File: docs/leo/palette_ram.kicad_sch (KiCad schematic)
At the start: 15 parts, among them IC10 74LS273, IC15 MB81C78A, IC16 MB81C78A, IC17 74153, IC18 74153, IC19 74153, IC22 74LS245, IC23 74LS245, IC25 74153, IC26 74153, IC27 74153, IC28 74153, IC30 74LS374, IC31 74LS374, IC9 74LS273

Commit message: Renamed shared ram
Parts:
- IC10, IC9: value 74LS273 -> (none)
- IC15, IC16: value MB81C78A -> (none); footprint Package_DIP:DIP-28_W15.24mm -> (none)
- IC17, IC18, IC19, IC25, IC26, IC27, IC28: value 74153 -> (none)
- IC22, IC23: value 74LS245 -> (none)
- IC30, IC31: value 74LS374 -> (none)
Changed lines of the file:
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@@
     (in_bom yes) (on_board yes) (fields_autoplaced)
     (property "Reference" "IC17" (id 0) (at 58.42 22.86 0))
-    (property "Value" "74153" (id 1) (at 58.42 25.4 0))
+    (property "Value" "" (id 1) (at 58.42 25.4 0))
     (property "Footprint" "" (id 2) (at 58.42 46.99 0)
       (effects (font (size 1.27 1.27)) hide)
@@
     (in_bom yes) (on_board yes) (fields_autoplaced)
     (property "Reference" "IC19" (id 0) (at 58.42 109.22 0))
-    (property "Value" "74153" (id 1) (at 58.42 111.76 0))
+    (property "Value" "" (id 1) (at 58.42 111.76 0))
     (property "Footprint" "" (id 2) (at 58.42 133.35 0)
       (effects (font (size 1.27 1.27)) hide)
@@
       (effects (font (size 1.27 1.27)) (justify right))
     )
-    (property "Value" "74LS273" (id 1) (at 258.3306 193.04 0)
+    (property "Value" "" (id 1) (at 258.3306 193.04 0)
       (effects (font (size 1.27 1.27)) (justify right))
     )
@@
       (effects (font (size 1.27 1.27)) (justify left))
     )
-    (property "Value" "74LS245" (id 1) (at 391.9094 48.26 0)
+    (property "Value" "" (id 1) (at 391.9094 48.26 0)
       (effects (font (size 1.27 1.27)) (justify left))
     )
@@
       (effects (font (size 1.27 1.27)) (justify right))
     )
-    (property "Value" "74LS374" (id 1) (at 390.4106 193.04 0)
+    (property "Value" "" (id 1) (at 390.4106 193.04 0)
       (effects (font (size 1.27 1.27)) (justify right))
     )
@@
       (effects (font (size 1.27 1.27)) (justify left))
     )
-    (property "Value" "MB81C78A" (id 1) (at 259.8294 48.26 0)
-      (effects (font (size 1.27 1.27)) (justify left))
-    )
-    (property "Footprint" "Package_DIP:DIP-28_W15.24mm" (id 2) (at 278.13 95.25 0)
+    (property "Value" "" (id 1) (at 259.8294 48.26 0)
+      (effects (font (size 1.27 1.27)) (justify left))
+    )
+    (property "Footprint" "" (id 2) (at 278.13 95.25 0)
       (effects (font (size 1.27 1.27)) hide)
     )
@@
       (effects (font (size 1.27 1.27)) (justify right))
     )
-    (property "Value" "74LS273" (id 1) (at 258.3306 246.38 0)
+    (property "Value" "" (id 1) (at 258.3306 246.38 0)
       (effects (font (size 1.27 1.27)) (justify right))
     )
@@
       (effects (font (size 1.27 1.27)) (justify left))
     )
-    (property "Value" "74LS245" (id 1) (at 391.9094 93.98 0)
+    (property "Value" "" (id 1) (at 391.9094 93.98 0)
       (effects (font (size 1.27 1.27)) (justify left))
     )
@@
     (in_bom yes) (on_board yes) (fields_autoplaced)
     (property "Reference" "IC28" (id 0) (at 133.35 152.4 0))
-    (property "Value" "74153" (id 1) (at 133.35 154.94 0))
+    (property "Value" "" (id 1) (at 133.35 154.94 0))
     (property "Footprint" "" (id 2) (at 133.35 176.53 0)
       (effects (font (size 1.27 1.27)) hide)
@@
     (in_bom yes) (on_board yes) (fields_autoplaced)
     (property "Reference" "IC18" (id 0) (at 58.42 66.04 0))
-    (property "Value" "74153" (id 1) (at 58.42 68.58 0))
+    (property "Value" "" (id 1) (at 58.42 68.58 0))
     (property "Footprint" "" (id 2) (at 58.42 90.17 0)
       (effects (font (size 1.27 1.27)) hide)
@@
       (effects (font (size 1.27 1.27)) hide)
     )
-    (property "Value" "GND" (id 1) (at 313.69 180.34 0))
+    (property "Value" "" (id 1) (at 313.69 180.34 0))
     (property "Footprint" "" (id 2) (at 313.69 175.26 0)
       (effects (font (size 1.27 1.27)) hide)
@@
     (in_bom yes) (on_board yes) (fields_autoplaced)
     (property "Reference" "IC27" (id 0) (at 133.35 109.22 0))
-    (property "Value" "74153" (id 1) (at 133.35 111.76 0))
+    (property "Value" "" (id 1) (at 133.35 111.76 0))
     (property "Footprint" "" (id 2) (at 133.35 133.35 0)
       (effects (font (size 1.27 1.27)) hide)
@@
       (effects (font (size 1.27 1.27)) (justify left))
     )
-    (property "Value" "MB81C78A" (id 1) (at 259.8294 116.84 0)
-      (effects (font (size 1.27 1.27)) (justify left))
-    )
-    (property "Footprint" "Package_DIP:DIP-28_W15.24mm" (id 2) (at 278.13 163.83 0)
+    (property "Value" "" (id 1) (at 259.8294 116.84 0)
+      (effects (font (size 1.27 1.27)) (justify left))
+    )
+    (property "Footprint" "" (id 2) (at 278.13 163.83 0)
       (effects (font (size 1.27 1.27)) hide)
     )
@@
       (effects (font (size 1.27 1.27)) hide)
     )
-    (property "Value" "GND" (id 1) (at 95.25 213.36 0))
+    (property "Value" "" (id 1) (at 95.25 213.36 0))
     (property "Footprint" "" (id 2) (at 95.25 208.28 0)
       (effects (font (size 1.27 1.27)) hide)
@@
     (in_bom yes) (on_board yes) (fields_autoplaced)
     (property "Reference" "IC26" (id 0) (at 133.35 66.04 0))
-    (property "Value" "74153" (id 1) (at 133.35 68.58 0))
+    (property "Value" "" (id 1) (at 133.35 68.58 0))
     (property "Footprint" "" (id 2) (at 133.35 90.17 0)
       (effects (font (size 1.27 1.27)) hide)
@@
       (effects (font (size 1.27 1.27)) hide)
     )
-    (property "Value" "VCC" (id 1) (at 223.52 33.02 0))
+    (property "Value" "" (id 1) (at 223.52 33.02 0))
     (property "Footprint" "" (id 2) (at 223.52 38.1 0)
       (effects (font (size 1.27 1.27)) hide)
@@
       (effects (font (size 1.27 1.27)) hide)
     )
-    (property "Value" "VCC" (id 1) (at 100.33 170.18 0))
+    (property "Value" "" (id 1) (at 100.33 170.18 0))
     (property "Footprint" "" (id 2) (at 100.33 175.26 0)
       (effects (font (size 1.27 1.27)) hide)
@@
       (effects (font (size 1.27 1.27)) (justify right))
     )
-    (property "Value" "74LS374" (id 1) (at 390.4106 147.32 0)
+    (property "Value" "" (id 1) (at 390.4106 147.32 0)
       (effects (font (size 1.27 1.27)) (justify right))
     )
@@
       (effects (font (size 1.27 1.27)) hide)
     )
-    (property "Value" "GND" (id 1) (at 22.86 213.36 0))
+    (property "Value" "" (id 1) (at 22.86 213.36 0))
     (property "Footprint" "" (id 2) (at 22.86 208.28 0)
       (effects (font (size 1.27 1.27)) hide)
@@
     (in_bom yes) (on_board yes) (fields_autoplaced)
     (property "Reference" "IC25" (id 0) (at 133.35 22.86 0))
-    (property "Value" "74153" (id 1) (at 133.35 25.4 0))
+    (property "Value" "" (id 1) (at 133.35 25.4 0))
     (property "Footprint" "" (id 2) (at 133.35 46.99 0)
       (effects (font (size 1.27 1.27)) hide)

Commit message: schematic updates
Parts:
- IC10, IC9: value (none) -> 74LS273
- IC15, IC16: value (none) -> MB81C78A; footprint (none) -> Package_DIP:DIP-28_W15.24mm
- IC17, IC18, IC19, IC25, IC26, IC27, IC28: value (none) -> 74153
- IC22, IC23: value (none) -> 74LS245
- IC30, IC31: value (none) -> 74LS374
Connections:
- net D0: now also IC30.19 (O7); no longer IC30.2 (O0)
- net D1: now also IC30.16 (O6); no longer IC30.5 (O1)
- net D10: now also IC31.15 (O5); no longer IC31.6 (O2)
- net D11: now also IC31.12 (O4); no longer IC31.9 (O3)
- net D12: now also IC31.9 (O3); no longer IC31.12 (O4)
- net D13: now also IC31.6 (O2); no longer IC31.15 (O5)
- net D14: now also IC31.5 (O1); no longer IC31.16 (O6)
- net D15: now also IC31.2 (O0); no longer IC31.19 (O7)
- net D2: now also IC30.15 (O5); no longer IC30.6 (O2)
- net D3: now also IC30.12 (O4); no longer IC30.9 (O3)
- net D4: now also IC30.9 (O3); no longer IC30.12 (O4)
- net D5: now also IC30.6 (O2); no longer IC30.15 (O5)
- net D6: now also IC30.5 (O1); no longer IC30.16 (O6)
- net D7: now also IC30.2 (O0); no longer IC30.19 (O7)
- net D8: now also IC31.19 (O7); no longer IC31.2 (O0)
- net D9: now also IC31.16 (O6); no longer IC31.5 (O1)
- net BUFFER_D11: now reaches IC31.13 (D4)
- net BUFFER_D10: now reaches IC31.14 (D5)
- net BUFFER_D9: now reaches IC31.17 (D6)
- net BUFFER_D8: now reaches IC31.18 (D7)
- net BUFFER_D15: now reaches IC31.3 (D0)
- net BUFFER_D14: now reaches IC31.4 (D1)
- net BUFFER_D13: now reaches IC31.7 (D2)
- net BUFFER_D12: now reaches IC31.8 (D3)
- net BUFFER_D3: now reaches IC30.13 (D4)
- net BUFFER_D2: now reaches IC30.14 (D5)
- net BUFFER_D1: now reaches IC30.17 (D6)
- net BUFFER_D0: now reaches IC30.18 (D7)
- net BUFFER_D7: now reaches IC30.3 (D0)
- net BUFFER_D6: now reaches IC30.4 (D1)
- net BUFFER_D5: now reaches IC30.7 (D2)
- net BUFFER_D4: now reaches IC30.8 (D3)
- net BUF_D0 renamed CPU_D0
- net BUF_D1 renamed CPU_D1
- net BUF_D10 renamed CPU_D10
- net BUF_D11 renamed CPU_D11
- net BUF_D12 renamed CPU_D12
- net BUF_D13 renamed CPU_D13
- net BUF_D14 renamed CPU_D14
- net BUF_D15 renamed CPU_D15
- net BUF_D2 renamed CPU_D2
- net BUF_D3 renamed CPU_D3
- net BUF_D4 renamed CPU_D4
- net BUF_D5 renamed CPU_D5
- net BUF_D6 renamed CPU_D6
- net BUF_D7 renamed CPU_D7
- net BUF_D8 renamed CPU_D8
- net BUF_D9 renamed CPU_D9

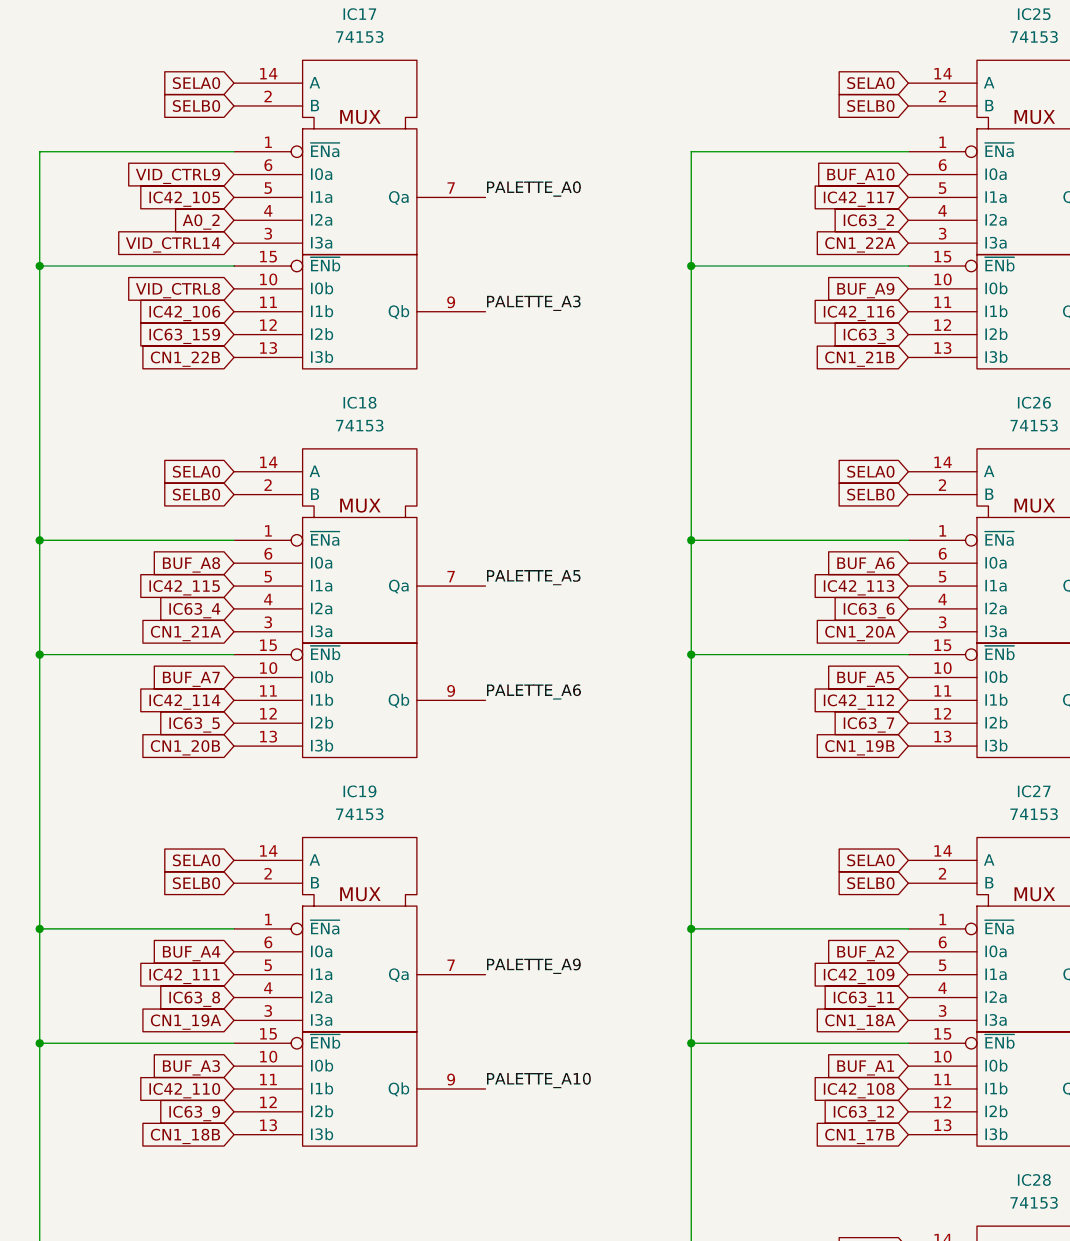
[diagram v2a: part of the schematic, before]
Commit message: Fixed up label names Added connectors sheet
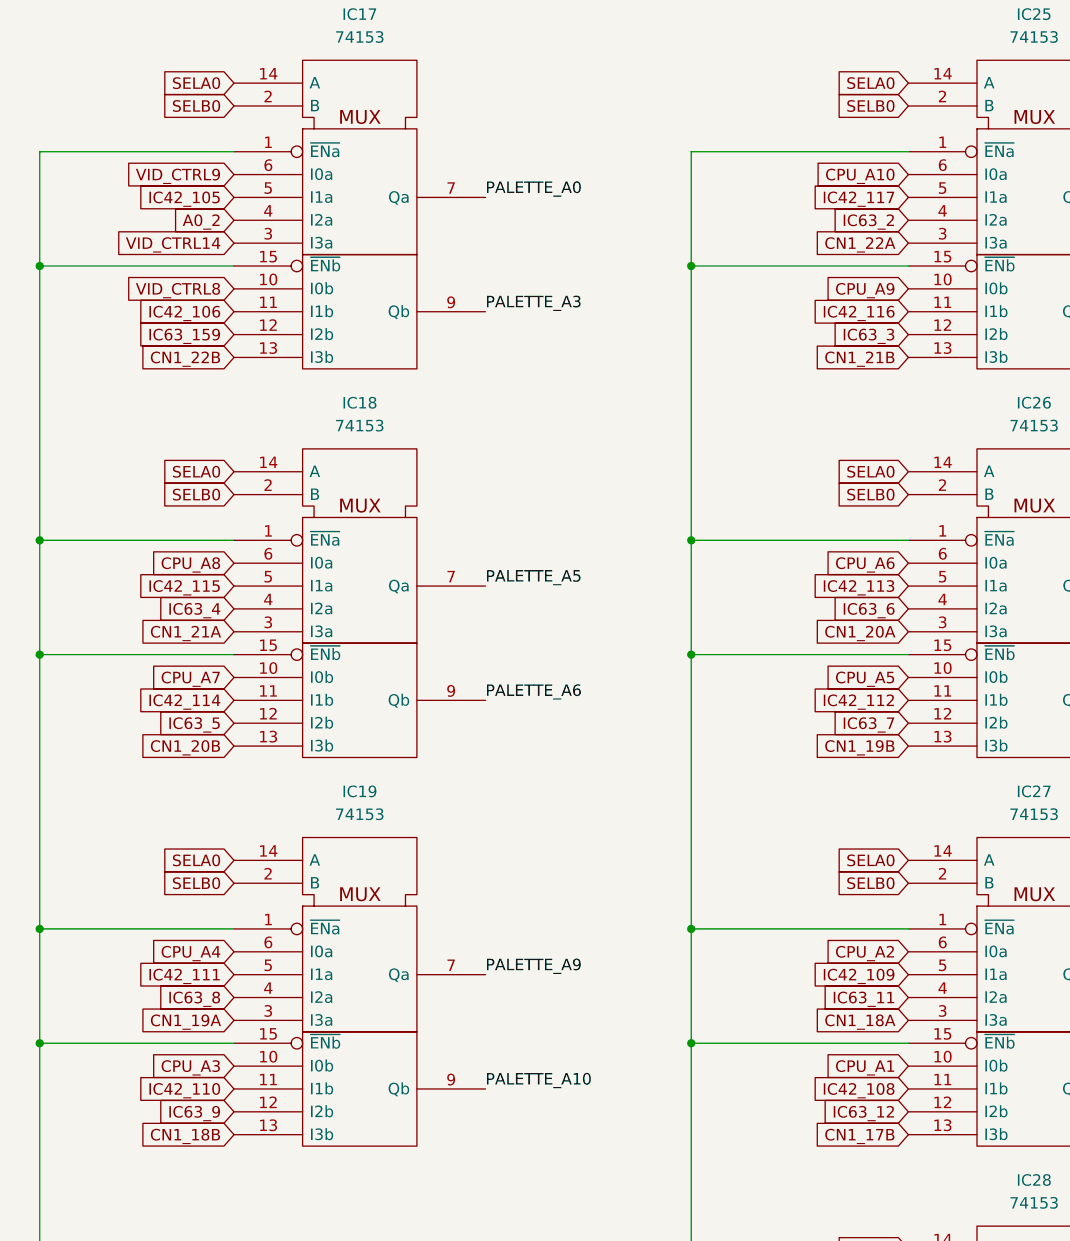
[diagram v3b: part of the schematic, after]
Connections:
- net BUF_A1 renamed CPU_A1
- net BUF_A10 renamed CPU_A10
- net BUF_A2 renamed CPU_A2
- net BUF_A3 renamed CPU_A3
- net BUF_A4 renamed CPU_A4
- net BUF_A5 renamed CPU_A5
- net BUF_A6 renamed CPU_A6
- net BUF_A7 renamed CPU_A7
- net BUF_A8 renamed CPU_A8
- net BUF_A9 renamed CPU_A9
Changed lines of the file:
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@@
     )
   )
-  (global_label "BUF_A9" (shape input) (at 119.38 53.34 180) (fields_autoplaced)
+  (global_label "CPU_A9" (shape input) (at 119.38 53.34 180) (fields_autoplaced)
     (effects (font (size 1.27 1.27)) (justify right))
     (property "Intersheet References" "${INTERSHEET_REFS}" (id 0) (at 110.0121 53.2606 0)
@@
     )
   )
-  (global_label "BUF_A6" (shape input) (at 119.38 83.82 180) (fields_autoplaced)
+  (global_label "CPU_A6" (shape input) (at 119.38 83.82 180) (fields_autoplaced)
     (effects (font (size 1.27 1.27)) (justify right))
     (property "Intersheet References" "${INTERSHEET_REFS}" (id 0) (at 110.0121 83.7406 0)
@@
     )
   )
-  (global_label "BUF_A8" (shape input) (at 44.45 83.82 180) (fields_autoplaced)
+  (global_label "CPU_A8" (shape input) (at 44.45 83.82 180) (fields_autoplaced)
     (effects (font (size 1.27 1.27)) (justify right))
     (property "Intersheet References" "${INTERSHEET_REFS}" (id 0) (at 35.0821 83.7406 0)
@@
     )
   )
-  (global_label "BUF_A1" (shape input) (at 119.38 139.7 180) (fields_autoplaced)
+  (global_label "CPU_A1" (shape input) (at 119.38 139.7 180) (fields_autoplaced)
     (effects (font (size 1.27 1.27)) (justify right))
     (property "Intersheet References" "${INTERSHEET_REFS}" (id 0) (at 110.0121 139.6206 0)
@@
     )
   )
-  (global_label "BUF_A10" (shape input) (at 119.38 40.64 180) (fields_autoplaced)
+  (global_label "CPU_A10" (shape input) (at 119.38 40.64 180) (fields_autoplaced)
     (effects (font (size 1.27 1.27)) (justify right))
     (property "Intersheet References" "${INTERSHEET_REFS}" (id 0) (at 108.8026 40.5606 0)
@@
     )
   )
-  (global_label "BUF_A4" (shape input) (at 44.45 127 180) (fields_autoplaced)
+  (global_label "CPU_A4" (shape input) (at 44.45 127 180) (fields_autoplaced)
     (effects (font (size 1.27 1.27)) (justify right))
     (property "Intersheet References" "${INTERSHEET_REFS}" (id 0) (at 35.0821 126.9206 0)
@@
     )
   )
-  (global_label "BUF_A3" (shape input) (at 44.45 139.7 180) (fields_autoplaced)
+  (global_label "CPU_A3" (shape input) (at 44.45 139.7 180) (fields_autoplaced)
     (effects (font (size 1.27 1.27)) (justify right))
     (property "Intersheet References" "${INTERSHEET_REFS}" (id 0) (at 35.0821 139.6206 0)
@@
     )
   )
-  (global_label "BUF_A5" (shape input) (at 119.38 96.52 180) (fields_autoplaced)
+  (global_label "CPU_A5" (shape input) (at 119.38 96.52 180) (fields_autoplaced)
     (effects (font (size 1.27 1.27)) (justify right))
     (property "Intersheet References" "${INTERSHEET_REFS}" (id 0) (at 110.0121 96.4406 0)
@@
     )
   )
-  (global_label "BUF_A7" (shape input) (at 44.45 96.52 180) (fields_autoplaced)
+  (global_label "CPU_A7" (shape input) (at 44.45 96.52 180) (fields_autoplaced)
     (effects (font (size 1.27 1.27)) (justify right))
     (property "Intersheet References" "${INTERSHEET_REFS}" (id 0) (at 35.0821 96.4406 0)
@@
     )
   )
-  (global_label "BUF_A2" (shape input) (at 119.38 127 180) (fields_autoplaced)
+  (global_label "CPU_A2" (shape input) (at 119.38 127 180) (fields_autoplaced)
     (effects (font (size 1.27 1.27)) (justify right))
     (property "Intersheet References" "${INTERSHEET_REFS}" (id 0) (at 110.0121 126.9206 0)
